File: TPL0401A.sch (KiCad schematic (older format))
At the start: 4 parts, among them J1 Conn_01x04_Male, J2 Conn_01x04_Male, U1 TPL0401A-10-Q1

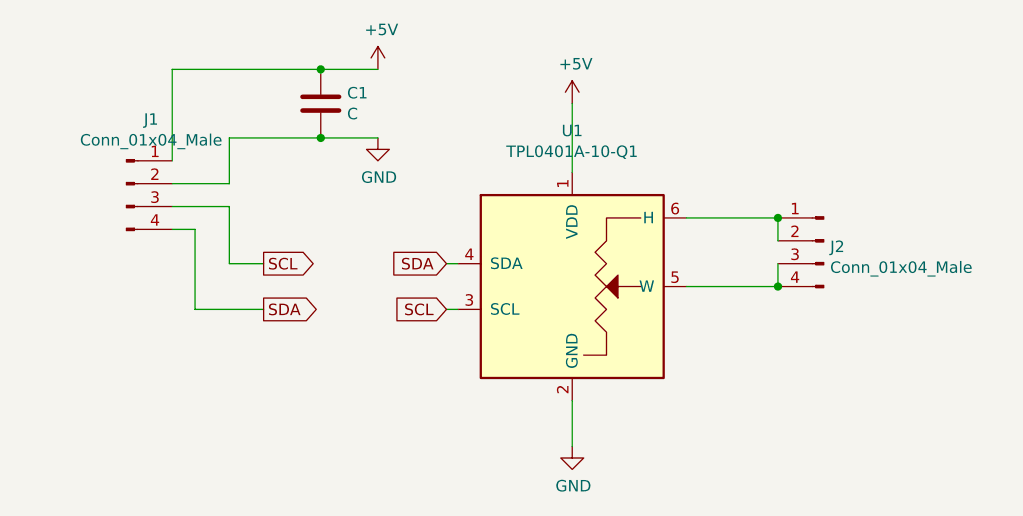
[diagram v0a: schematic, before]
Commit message: TPL0401A: Pull up SCL and SDA in PCB
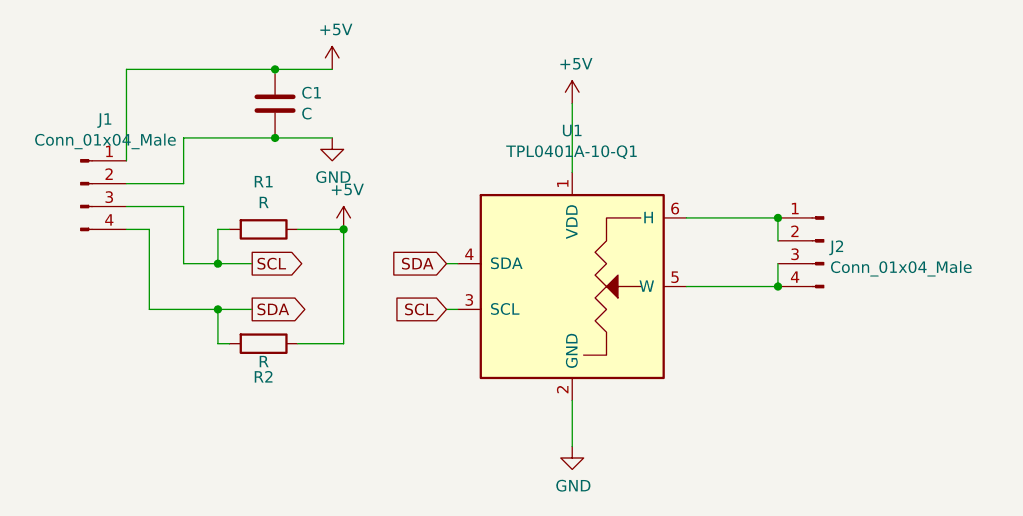
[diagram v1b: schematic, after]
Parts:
- added R1, R2: R, Resistor_SMD:R_0805_2012Metric, symbol Device:R
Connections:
- net +5V: now also R1.1, R2.1
- net SCL: now also R1.2
- net SDA: now also R2.2
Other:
- moved on the sheet: C1, J1
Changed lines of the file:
@@
 L Connector:Conn_01x04_Male J1
 U 1 1 60D5B895
-P 3600 2400
-F 0 "J1" H 3708 2681 50  0000 C CNN
-F 1 "Conn_01x04_Male" H 3708 2590 50  0000 C CNN
-F 2 "Connector_PinHeader_2.54mm:PinHeader_1x04_P2.54mm_Vertical" H 3600 2400 50  0001 C CNN
-F 3 "~" H 3600 2400 50  0001 C CNN
-	1    3600 2400
+P 3400 2400
+F 0 "J1" H 3508 2681 50  0000 C CNN
+F 1 "Conn_01x04_Male" H 3508 2590 50  0000 C CNN
+F 2 "Connector_PinHeader_2.54mm:PinHeader_1x04_P2.54mm_Vertical" H 3400 2400 50  0001 C CNN
+F 3 "~" H 3400 2400 50  0001 C CNN
+	1    3400 2400
 	1    0    0    -1
 $EndComp
@@
 L power:+5V #PWR01
 U 1 1 60D5F5B2
-P 4700 1900
-F 0 "#PWR01" H 4700 1750 50  0001 C CNN
-F 1 "+5V" H 4715 2073 50  0000 C CNN
-F 2 "" H 4700 1900 50  0001 C CNN
-F 3 "" H 4700 1900 50  0001 C CNN
-	1    4700 1900
+P 4500 1900
+F 0 "#PWR01" H 4500 1750 50  0001 C CNN
+F 1 "+5V" H 4515 2073 50  0000 C CNN
+F 2 "" H 4500 1900 50  0001 C CNN
+F 3 "" H 4500 1900 50  0001 C CNN
+	1    4500 1900
 	1    0    0    -1
 $EndComp
@@
 L power:GND #PWR02
 U 1 1 60D5FA4F
-P 4700 2200
-F 0 "#PWR02" H 4700 1950 50  0001 C CNN
-F 1 "GND" H 4705 2027 50  0000 C CNN
-F 2 "" H 4700 2200 50  0001 C CNN
-F 3 "" H 4700 2200 50  0001 C CNN
-	1    4700 2200
+P 4500 2200
+F 0 "#PWR02" H 4500 1950 50  0001 C CNN
+F 1 "GND" H 4505 2027 50  0000 C CNN
+F 2 "" H 4500 2200 50  0001 C CNN
+F 3 "" H 4500 2200 50  0001 C CNN
+	1    4500 2200
 	1    0    0    -1
 $EndComp
@@
 Text GLabel 5000 2950 0    50   Input ~ 0
 SCL
-Text GLabel 4200 2750 2    50   Output ~ 0
+Text GLabel 4150 2750 2    50   Output ~ 0
 SCL
-Text GLabel 4200 2950 2    50   Output ~ 0
+Text GLabel 4150 2950 2    50   Output ~ 0
 SDA
 $Comp
 L Device:C C1
 U 1 1 60D62721
-P 4450 2050
-F 0 "C1" H 4565 2096 50  0000 L CNN
-F 1 "C" H 4565 2005 50  0000 L CNN
-F 2 "Capacitor_SMD:C_0805_2012Metric" H 4488 1900 50  0001 C CNN
-F 3 "~" H 4450 2050 50  0001 C CNN
-	1    4450 2050
+P 4250 2050
+F 0 "C1" H 4365 2096 50  0000 L CNN
+F 1 "C" H 4365 2005 50  0000 L CNN
+F 2 "Capacitor_SMD:C_0805_2012Metric" H 4288 1900 50  0001 C CNN
+F 3 "~" H 4250 2050 50  0001 C CNN
+	1    4250 2050
 	1    0    0    -1
 $EndComp
 Wire Wire Line
-	4700 1900 4450 1900
+	4500 1900 4250 1900
 Wire Wire Line
-	4450 1900 3800 1900
+	4250 1900 3600 1900
 Wire Wire Line
-	3800 1900 3800 2300
-Connection ~ 4450 1900
+	3600 1900 3600 2300
+Connection ~ 4250 1900
 Wire Wire Line
-	4700 2200 4450 2200
+	4500 2200 4250 2200
 Wire Wire Line
-	4450 2200 4050 2200
+	4250 2200 3850 2200
 Wire Wire Line
-	4050 2200 4050 2400
+	3850 2200 3850 2400
 Wire Wire Line
-	4050 2400 3800 2400
-Connection ~ 4450 2200
+	3850 2400 3600 2400
+Connection ~ 4250 2200
 Wire Wire Line
-	4200 2750 4050 2750
+	3850 2750 3850 2500
 Wire Wire Line
-	4050 2750 4050 2500
+	3850 2500 3600 2500
 Wire Wire Line
-	4050 2500 3800 2500
+	3700 2950 3700 2600
 Wire Wire Line
-	4200 2950 3900 2950
-Wire Wire Line
-	3900 2950 3900 2600
-Wire Wire Line
-	3900 2600 3800 2600
+	3700 2600 3600 2600
 Wire Wire Line
 	5050 2750 5000 2750
@@
 	6450 2850 6050 2850
 Connection ~ 6450 2850
+$Comp
+L power:+5V #PWR0101
+U 1 1 60D5D775
+P 4550 2600
+F 0 "#PWR0101" H 4550 2450 50  0001 C CNN
+F 1 "+5V" H 4565 2773 50  0000 C CNN
+F 2 "" H 4550 2600 50  0001 C CNN
+F 3 "" H 4550 2600 50  0001 C CNN
+	1    4550 2600
+	1    0    0    -1
+$EndComp
+$Comp
+L Device:R R1
+U 1 1 60D60549
+P 4200 2600
+F 0 "R1" V 3993 2600 50  0000 C CNN
+F 1 "R" V 4084 2600 50  0000 C CNN
+F 2 "Resistor_SMD:R_0805_2012Metric" V 4130 2600 50  0001 C CNN
+F 3 "~" H 4200 2600 50  0001 C CNN
+	1    4200 2600
+	0    1    1    0
+$EndComp
+$Comp
+L Device:R R2
+U 1 1 60D5F6F4
+P 4200 3100
+F 0 "R2" V 4347 3100 50  0000 C CNN
+F 1 "R" V 4280 3100 50  0000 C CNN
+F 2 "Resistor_SMD:R_0805_2012Metric" V 4130 3100 50  0001 C CNN
+F 3 "~" H 4200 3100 50  0001 C CNN
+	1    4200 3100
+	0    1    1    0
+$EndComp
+Wire Wire Line
+	3850 2750 4000 2750
+Wire Wire Line
+	3700 2950 4000 2950
+Wire Wire Line
+	4050 3100 4000 3100
+Wire Wire Line
+	4000 3100 4000 2950
+Connection ~ 4000 2950
+Wire Wire Line
+	4000 2950 4150 2950
+Wire Wire Line
+	4050 2600 4000 2600
+Wire Wire Line
+	4000 2600 4000 2750
+Connection ~ 4000 2750
+Wire Wire Line
+	4000 2750 4150 2750
+Wire Wire Line
+	4350 2600 4550 2600
+Wire Wire Line
+	4350 3100 4550 3100
+Wire Wire Line
+	4550 3100 4550 2600
+Connection ~ 4550 2600
 $EndSCHEMATC
